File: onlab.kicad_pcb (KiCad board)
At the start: 2 copper layers, 100 x 100 mm, 82 parts, among them J1 Battery, J10 DC-Motor, J2 HC_SR04, J3 HC_SR04, J4 HC_SR04, J5 DC-Motor, J6 DC-Motor, J7 DC-Motor, J8 DC-Motor, J9 DC-Motor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

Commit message: layout v2
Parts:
- added F1: MountingHole_3.2mm_M3, MountingHole:MountingHole_3.2mm_M3, F.Cu at (122.1, 34.9)
- added F2: MountingHole_3.2mm_M3, MountingHole:MountingHole_3.2mm_M3, F.Cu at (206.4, 34.6)
- added F3: MountingHole_3.2mm_M3, MountingHole:MountingHole_3.2mm_M3, F.Cu at (122.1, 119.2)
- added F4: MountingHole_3.2mm_M3, MountingHole:MountingHole_3.2mm_M3, F.Cu at (206.4, 118.9)
- J10, J8, J9: footprint Connector_Molex:Molex_KK-254_AE-6410-06A_1x06_P2.54mm_Vertical -> Onlab:motor
- moved C6 161.6 mm to (189.5, 54.2)
- moved J4 161.6 mm to (211.2, 81.1), turned to 180 degrees
- moved C4 161.4 mm to (196.5, 114.3), turned to 180 degrees
- moved C3 154.3 mm to (189.1, 114.2), turned to 180 degrees
- moved C7 150.1 mm to (185.5, 96.0), turned to -90 degrees
- moved C2 147.2 mm to (181.5, 114.2), turned to 180 degrees
- moved J2 141.2 mm to (168.4, 30.4), turned to -90 degrees
- moved C8 140.6 mm to (163.7, 52.1)
- moved U3 137.9 mm to (193.5, 47.0), turned to 180 degrees
- moved U4 130.0 mm to (192.8, 100.1), turned to 90 degrees
- moved R20 127.9 mm to (205.4, 46.4)
- moved U1 127.0 mm to (158.2, 88.5), turned to 180 degrees
- moved C9 125.9 mm to (161.7, 108.1)
- moved R19 125.7 mm to (205.4, 50.2)
- moved R18 123.8 mm to (205.4, 54.0)
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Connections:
- R10 pad 1: Net-(U4-P5) -> Net-(U4-P7)
- R12 pad 1: Net-(U4-P7) -> Net-(U4-P5)
- SW3 pad 1: Net-(U4-P5) -> Net-(U4-P7)
- SW3 pad 3: Net-(U4-P7) -> Net-(U4-P5)

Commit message: Routing
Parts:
- moved R5 6.14 mm to (118.6, 107.1), turned to 0 degrees
- moved R22 6.06 mm to (123.4, 107.1), turned to 0 degrees
- moved SW3 4.95 mm to (193.3, 74.4)
- moved SW2 4.56 mm to (150.6, 41.7), turned to 90 degrees
- moved SW1 3.61 mm to (141.6, 41.5), turned to 90 degrees
- moved R4 2.92 mm to (118.6, 102.6)
- moved R3 2.92 mm to (123.4, 102.6)
- moved R16 1.55 mm to (169.3, 122.6)
- moved C4 1.53 mm to (198.0, 114.2)
- moved R15 1.45 mm to (199.0, 110.1)
- moved R14 1.31 mm to (191.4, 110.0)
- moved C3 1.27 mm to (190.4, 114.2)
- moved C2 1.25 mm to (182.7, 114.2)
- moved R13 1.20 mm to (183.8, 110.1)
- moved Q2 0.90 mm to (122.6, 70.0)
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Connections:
- U5 pad 13: /Mot3_DrvA -> /Mot2_DrvA
- U5 pad 15: /Mot3_DrvB -> /Mot2_DrvB
- U5 pad 24: /Mot2_DrvB -> /Mot3_DrvB
- U5 pad 25: /Mot2_DrvA -> /Mot3_DrvA
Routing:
- net +5V: track 0.00 -> 264.3 mm, vias 0 -> 1
- net +3.3V: track 0.00 -> 35.7 mm
- net Net-(D1-A): track 0.00 -> 21.3 mm
- net /LED_5: track 0.00 -> 17.8 mm
- net VCC: track 0.00 -> 17.4 mm
- net /LED_1: track 0.00 -> 14.4 mm
- net Net-(U5-EN/RESET): track 0.00 -> 14.4 mm
- net Net-(JP1-C): track 0.00 -> 14.0 mm
- net Net-(D2-A2): track 0.00 -> 13.6 mm
- net /Battery level: track 0.00 -> 12.0 mm
- net /LED_2: track 0.00 -> 11.0 mm
- net /LED_3: track 0.00 -> 9.31 mm
- net Net-(J4-Pin_2): track 0.00 -> 8.10 mm
- net Net-(J2-Pin_2): track 0.00 -> 7.60 mm
- net Net-(J3-Pin_2): track 0.00 -> 7.41 mm
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
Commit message: Routing part 2
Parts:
- moved R8 14.4 mm to (166.5, 48.1)
- moved C8 13.7 mm to (172.0, 63.0), turned to 180 degrees
- moved U7 5.86 mm to (171.5, 54.0), turned to 90 degrees
- moved D2 0.92 mm to (131.3, 39.9)
- moved SW2 0.92 mm to (150.8, 42.6)
- moved D1 0.92 mm to (132.0, 45.6)
- moved D3 0.92 mm to (153.4, 30.2)
- moved D4 0.92 mm to (143.4, 30.2)
- moved F1 0.92 mm to (134.7, 33.5)
- moved J1 0.92 mm to (131.2, 32.5)
- moved R2 0.92 mm to (143.4, 32.9)
- moved SW1 0.92 mm to (141.7, 42.4)
- moved R1 0.92 mm to (153.4, 32.9)
- moved U2 0.92 mm to (139.3, 55.5)
- moved Q3 0.87 mm to (205.2, 84.4)
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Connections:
- U5 pad 10: /Mot1_DrvB -> /Mot1_DrvA
- U5 pad 13: /Mot2_DrvA -> /Mot3_EncA
- U5 pad 15: /Mot2_DrvB -> /Mot3_EncB
- U5 pad 3: /Mot3_EncA -> /Mot1_EncA
- U5 pad 4: /Mot3_EncB -> /Mot1_EncB
- U5 pad 5: /Mot1_EncA -> /Mot2_EncA
- U5 pad 6: /Mot1_EncB -> /Mot2_EncB
- U5 pad 7: /Mot2_EncA -> /Mot2_DrvB
- U5 pad 8: /Mot2_EncB -> /Mot2_DrvA
- U5 pad 9: /Mot1_DrvA -> /Mot1_DrvB
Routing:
- net +3.3V: track 35.7 -> 342.2 mm
- net /Mot2_EncB: track 0.00 -> 109.0 mm
- net /Mot2_EncA: track 0.00 -> 104.9 mm
- net /Mot2_DrvB: track 0.00 -> 85.8 mm
- net /Mot2_DrvA: track 0.00 -> 84.6 mm
- net /Mot1_DrvB: track 0.00 -> 77.2 mm
- net /Mot1_DrvA: track 0.00 -> 75.7 mm
- net /Mot1_EncB: track 0.00 -> 53.9 mm
- net /Mot1_EncA: track 0.00 -> 48.0 mm
- net Net-(U7-EEP): track 3.81 -> 0.00 mm
- net +5V: track 264.3 -> 261.0 mm
- net VCC: track 17.4 -> 15.1 mm

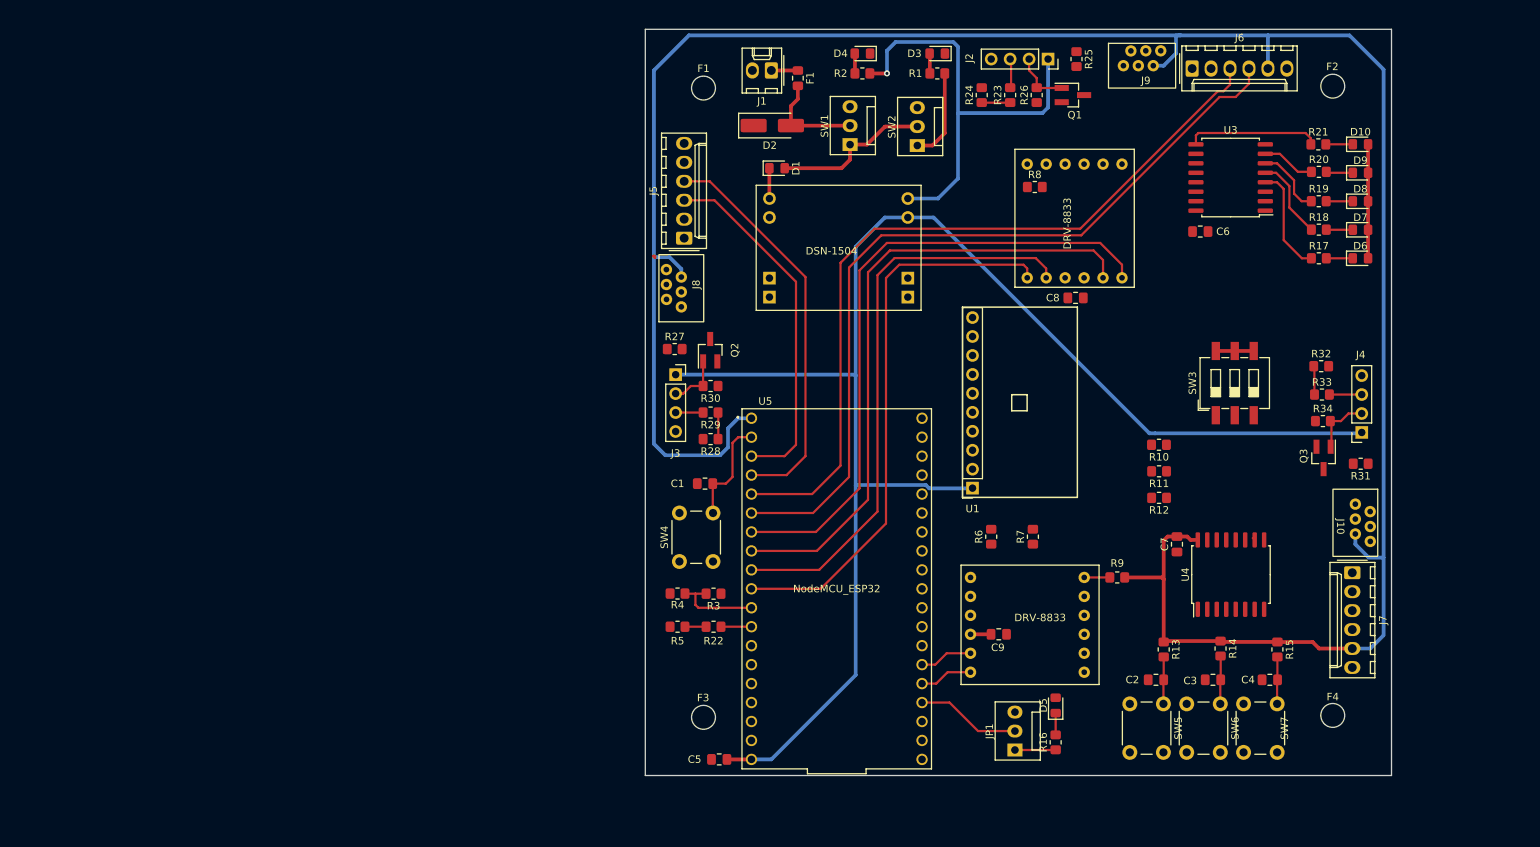
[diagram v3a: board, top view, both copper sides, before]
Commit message: Routing part 3 - remain to be done motors and vcc
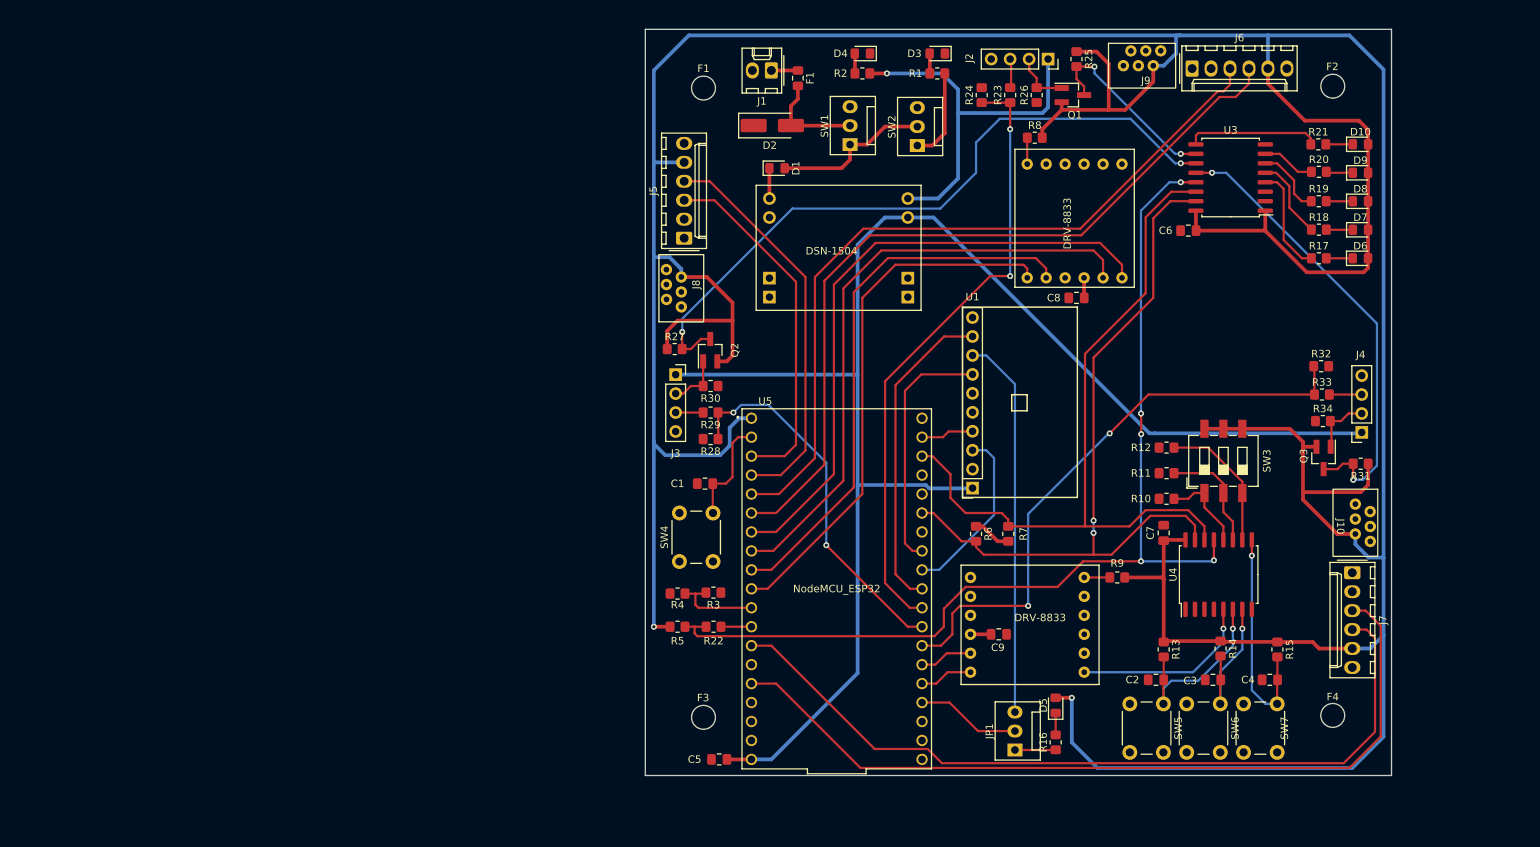
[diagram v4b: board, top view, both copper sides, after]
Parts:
- moved SW3 10.5 mm to (191.8, 84.8)
- moved R10 7.31 mm to (184.2, 89.9)
- moved R12 6.80 mm to (184.2, 83.1)
- moved R8 6.60 mm to (166.5, 41.5)
- moved R7 3.32 mm to (162.9, 94.6)
- moved C7 2.34 mm to (183.8, 94.5), turned to 90 degrees
- moved R6 2.07 mm to (158.6, 94.6), turned to -90 degrees
- moved U4 1.65 mm to (191.1, 100.1)
- moved C6 1.61 mm to (187.1, 54.0), turned to 180 degrees
- moved R11 1.03 mm to (184.2, 86.5)
- moved R3 0.14 mm to (123.4, 102.5)
- moved C8 0.13 mm to (172.1, 63.0)
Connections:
- U5 pad 13: /Mot3_EncA -> /Mot3_EncB
- U5 pad 15: /Mot3_EncB -> /Mot3_EncA
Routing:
- net +3.3V: track 342.2 -> 597.0 mm, vias 0 -> 2
- net /Interrupt: track 2.83 -> 138.4 mm, vias 0 -> 5
- net /Mot3_EncA: track 0.00 -> 110.3 mm
- net /Mot3_EncB: track 0.00 -> 107.9 mm
- net /I2C_SCL: track 0.00 -> 100.7 mm
- net /I2C_SDA: track 0.00 -> 99.3 mm, vias 0 -> 2
- net /UV_Trig_2: track 0.00 -> 93.6 mm, vias 0 -> 2
- net /UV_Echo_1: track 3.82 -> 83.1 mm, vias 0 -> 2
- net /UV_Echo_3: track 3.84 -> 79.7 mm, vias 0 -> 2
- net /UV_Trig_3: track 0.00 -> 62.2 mm, vias 0 -> 2
- net /MPU95 interrupt: track 0.00 -> 51.2 mm
- net /UV_Echo_2: track 3.74 -> 50.3 mm, vias 0 -> 2
- net /nCS: track 0.00 -> 42.7 mm
- net /MISO: track 0.00 -> 33.1 mm
- net /UV_Trig_1: track 0.00 -> 25.7 mm, vias 0 -> 2
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
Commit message: Routing part 4 - remain to be done GND and GNDPWR
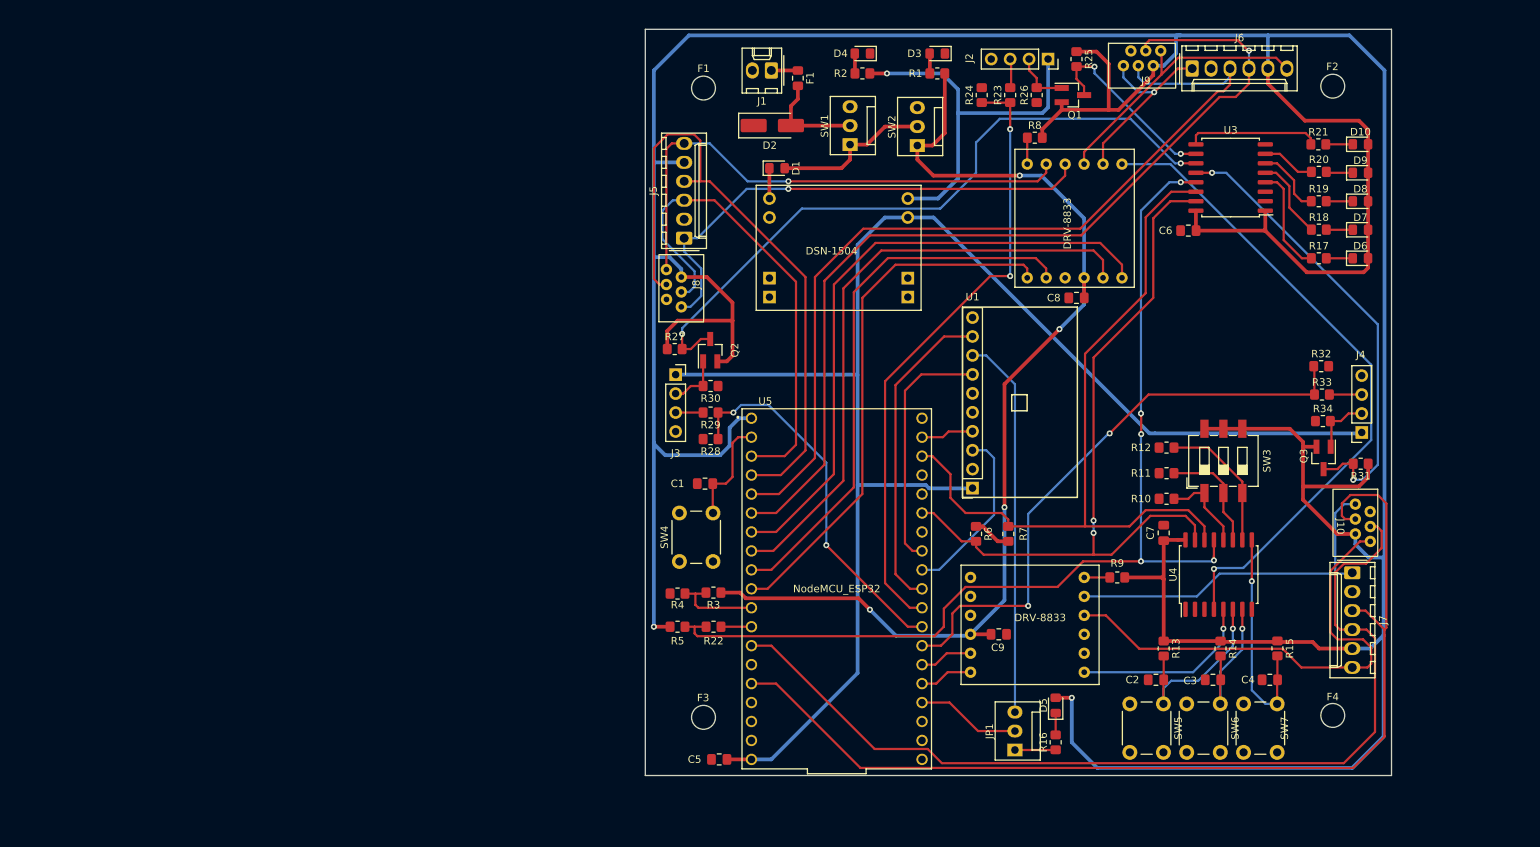
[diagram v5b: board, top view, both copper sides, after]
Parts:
- moved R15 0.14 mm to (199.0, 110.0)
- moved R13 0.13 mm to (183.8, 110.0)
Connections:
- U7 pad 10: /Mot1_B -> /Mot1_A
- U7 pad 11: /Mot1_A -> /Mot1_B
- U7 pad 8: /Mot2_B -> /Mot2_A
- U7 pad 9: /Mot2_A -> /Mot2_B
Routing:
- net VCC: track 17.8 -> 143.3 mm, vias 0 -> 4
- net /DRV1_FAULT: track 0.00 -> 88.4 mm, vias 0 -> 1
- net /Mot1_B: track 0.00 -> 71.1 mm, vias 0 -> 1
- net /Mot1_A: track 0.00 -> 68.0 mm, vias 0 -> 1
- net /Mot3_B: track 0.00 -> 65.2 mm
- net /Mot3_A: track 0.00 -> 48.4 mm
- net /Mot2_B: track 0.00 -> 37.9 mm
- net /Mot1_EncB: track 53.4 -> 85.7 mm
- net /Mot3_EncA: track 110.3 -> 138.5 mm
- net /Mot2_A: track 0.00 -> 25.4 mm, vias 0 -> 1
- net /Mot3_EncB: track 107.9 -> 129.1 mm
- net /Mot2_EncB: track 107.0 -> 125.1 mm, vias 0 -> 1
- net /Mot1_EncA: track 48.0 -> 65.5 mm
- net /Mot2_EncA: track 103.2 -> 118.9 mm
- net +3.3V: track 597.0 -> 595.6 mm
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
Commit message: Layout finish
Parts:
- moved C8 1.40 mm to (172.0, 64.4)
- moved R22 0.13 mm to (123.4, 107.2)
- moved R5 0.13 mm to (118.6, 107.2)
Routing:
- net GNDPWR: track 0.00 -> 215.3 mm, vias 0 -> 7
- net GND: track 0.00 -> 28.5 mm, vias 0 -> 35
- net +3.3V: track 595.6 -> 618.6 mm, vias 2 -> 4
- net +5V: track 252.3 -> 265.8 mm, vias 1 -> 4
- net /Button_2: track 20.4 -> 26.9 mm
- net Net-(U5-EN/RESET): track 14.4 -> 20.9 mm
- net /Button_3: track 30.8 -> 37.3 mm
- net /Button_1: track 25.1 -> 31.5 mm
- net Net-(D1-K): track 4.07 -> 6.61 mm
- net VCC: track 143.3 -> 144.7 mm
- net /I2C_SCL: track 100.7 -> 101.7 mm
- net /I2C_SDA: track 99.3 -> 98.4 mm
- net /UV_Trig_2: track 92.8 -> 92.0 mm
- net /Mot3_EncA: track 138.5 -> 139.3 mm
- net /UV_Echo_3: track 79.7 -> 78.9 mm
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- added copper zone on B.Cu, net GND
- added copper zone on F.Cu, net GND
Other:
- rule pad_to_mask_clearance: 0 -> 0.038
- board text added: "+3.3V"
- board text added: "+5V"
- board text added: "Echo1"
- board text added: "Echo2"
- board text added: "Echo3"
- board text added: "Enc1_A"
- board text added: "Enc1_B"
- board text added: "Enc2_A"
- board text added: "Enc2_B"
- board text added: "Enc3_A"
- board text added: "Enc3_B"
- board text added: "GND"
- board text added: "Input+"
- board text added: "Input-"
- board text added: "Mot1_A"
- board text added: "Mot1_B"
- board text added: "Mot2_A"
- board text added: "Mot2_B"
- board text added: "Mot3_A"
- board text added: "Mot3_B"
- board text added: "Output+"
- board text added: "Output-"
- board text added: "Trig1"
- board text added: "Trig2"
- board text added: "Trig3"
